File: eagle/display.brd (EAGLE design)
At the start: 100 x 20 mm, 6 parts

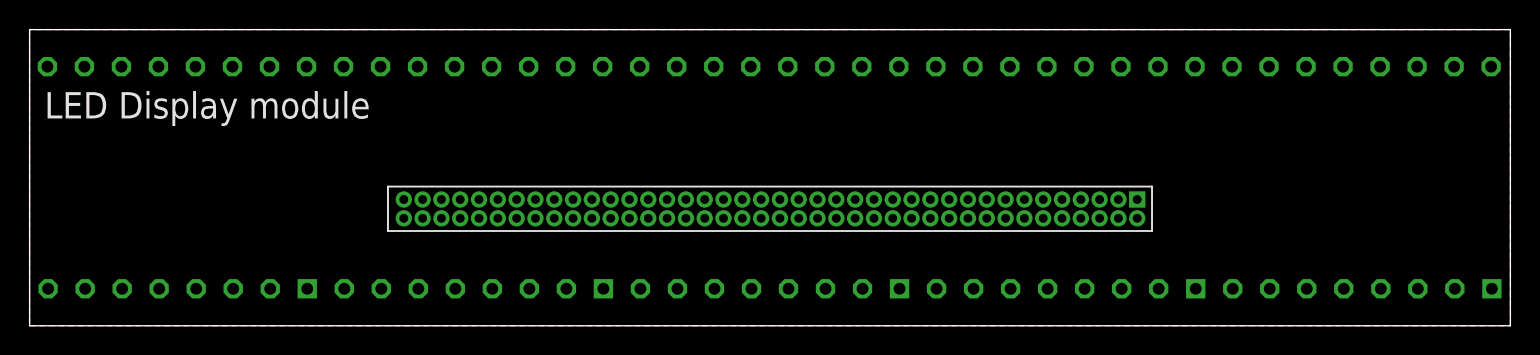
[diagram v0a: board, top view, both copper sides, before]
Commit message: removed pinhead
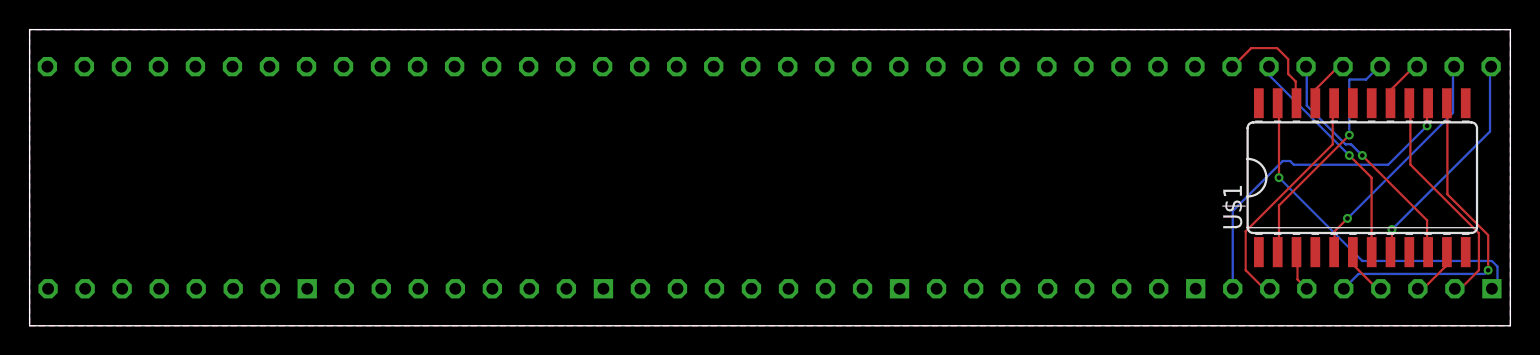
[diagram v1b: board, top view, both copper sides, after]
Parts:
- removed U$6: PINHD-2X40FEMALE, pinhead-1.27:FEMALE-2X40
- added U$1: MAX7219CWG, max7219:SO24L
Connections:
- removed net MX1_ANODE1: U$6.P$1
- removed net MX1_ANODE2: U$6.P$3
- removed net MX1_ANODE3: U$6.P$5
- removed net MX1_ANODE4: U$6.P$7
- removed net MX1_ANODE5: U$6.P$9
- removed net MX1_ANODE6: U$6.P$11
- removed net MX1_ANODE7: U$6.P$13
- removed net MX1_ANODE8: U$6.P$15
- removed net MX1_CATHODE1: U$6.P$2
- removed net MX1_CATHODE2: U$6.P$4
- removed net MX1_CATHODE3: U$6.P$6
- removed net MX1_CATHODE4: U$6.P$8
- removed net MX1_CATHODE5: U$6.P$10
- removed net MX1_CATHODE6: U$6.P$12
- removed net MX1_CATHODE7: U$6.P$14
- removed net MX1_CATHODE8: U$6.P$16
- removed net MX2_ANODE1: U$6.P$17
- removed net MX2_ANODE2: U$6.P$19
- removed net MX2_ANODE3: U$6.P$21
- removed net MX2_ANODE4: U$6.P$23
- removed net MX2_ANODE5: U$6.P$25
- removed net MX2_ANODE6: U$6.P$27
- removed net MX2_ANODE7: U$6.P$29
- removed net MX2_ANODE8: U$6.P$31
- removed net MX2_CATHODE1: U$6.P$18
- removed net MX2_CATHODE2: U$6.P$20
- removed net MX2_CATHODE3: U$6.P$22
- removed net MX2_CATHODE4: U$6.P$24
- removed net MX2_CATHODE5: U$6.P$26
- removed net MX2_CATHODE6: U$6.P$28
- removed net MX2_CATHODE7: U$6.P$30
- removed net MX2_CATHODE8: U$6.P$32
- removed net MX3_ANODE1: U$6.P$33
- removed net MX3_ANODE2: U$6.P$35
- removed net MX3_ANODE3: U$6.P$37
- removed net MX3_ANODE4: U$6.P$39
- removed net MX3_ANODE5: U$6.P$41
- removed net MX3_ANODE6: U$6.P$43
- removed net MX3_ANODE7: U$6.P$45
- removed net MX3_ANODE8: U$6.P$47
- removed net MX3_CATHODE1: U$6.P$34
- removed net MX3_CATHODE2: U$6.P$36
- removed net MX3_CATHODE3: U$6.P$38
- removed net MX3_CATHODE4: U$6.P$40
- removed net MX3_CATHODE5: U$6.P$42
- removed net MX3_CATHODE6: U$6.P$44
- removed net MX3_CATHODE7: U$6.P$46
- removed net MX3_CATHODE8: U$6.P$48
- removed net MX4_ANODE1: U$6.P$49
- removed net MX4_ANODE2: U$6.P$51
- removed net MX4_ANODE3: U$6.P$53
- removed net MX4_ANODE4: U$6.P$55
- removed net MX4_ANODE5: U$6.P$57
- removed net MX4_ANODE6: U$6.P$59
- removed net MX4_ANODE7: U$6.P$61
- removed net MX4_ANODE8: U$6.P$63
- removed net MX4_CATHODE1: U$6.P$50
- removed net MX4_CATHODE2: U$6.P$52
- removed net MX4_CATHODE3: U$6.P$54
- removed net MX4_CATHODE4: U$6.P$56
- removed net MX4_CATHODE5: U$6.P$58
- removed net MX4_CATHODE6: U$6.P$60
- removed net MX4_CATHODE7: U$6.P$62
- removed net MX4_CATHODE8: U$6.P$64
- removed net MX5_ANODE1: U$6.P$65
- removed net MX5_ANODE2: U$6.P$67
- removed net MX5_ANODE3: U$6.P$69
- removed net MX5_ANODE4: U$6.P$71
- removed net MX5_ANODE5: U$6.P$73
- removed net MX5_ANODE6: U$6.P$75
- removed net MX5_ANODE7: U$6.P$77
- removed net MX5_ANODE8: U$6.P$79
- removed net MX5_CATHODE1: U$6.P$66
- removed net MX5_CATHODE2: U$6.P$68
- removed net MX5_CATHODE3: U$6.P$70
- removed net MX5_CATHODE4: U$6.P$72
- removed net MX5_CATHODE5: U$6.P$74
- removed net MX5_CATHODE6: U$6.P$76
- removed net MX5_CATHODE7: U$6.P$78
- removed net MX5_CATHODE8: U$6.P$80
- new net ANODE1: LED1.P$5, U$1.14
- new net ANODE2: LED1.P$2, U$1.16
- new net ANODE3: LED1.P$7, U$1.20
- new net ANODE4: LED1.P$1, U$1.23
- new net ANODE5: LED1.P$12, U$1.21
- new net ANODE6: LED1.P$8, U$1.15
- new net ANODE7: LED1.P$14, U$1.17
- new net ANODE8: LED1.P$9, U$1.22
- new net CATHODE1: LED1.P$13, U$1.2
- new net CATHODE2: LED1.P$3, U$1.11
- new net CATHODE3: LED1.P$4, U$1.6
- new net CATHODE4: LED1.P$10, U$1.7
- new net CATHODE5: LED1.P$6, U$1.3
- new net CATHODE6: LED1.P$11, U$1.10
- new net CATHODE7: LED1.P$15, U$1.5
- new net CATHODE8: LED1.P$16, U$1.8
- new net GND: U$1.4, U$1.9
- new net VCC: U$1.19
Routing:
- net ANODE4: track 0.00 -> 24.2 mm, vias 0 -> 1
- net ANODE1: track 0.00 -> 22.7 mm, vias 0 -> 1
- net ANODE6: track 0.00 -> 22.5 mm, vias 0 -> 1
- net CATHODE6: track 0.00 -> 16.2 mm, vias 0 -> 1
- net CATHODE1: track 0.00 -> 16.1 mm, vias 0 -> 1
- net CATHODE7: track 0.00 -> 15.9 mm, vias 0 -> 1
- net ANODE3: track 0.00 -> 15.9 mm
- net CATHODE4: track 0.00 -> 15.4 mm, vias 0 -> 1
- net CATHODE8: track 0.00 -> 15.4 mm, vias 0 -> 1
- net ANODE2: track 0.00 -> 15.4 mm
- net ANODE8: track 0.00 -> 7.82 mm
- net CATHODE2: track 0.00 -> 3.50 mm
- net ANODE5: track 0.00 -> 3.43 mm
- net CATHODE3: track 0.00 -> 3.39 mm
- net ANODE7: track 0.00 -> 3.33 mm
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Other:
- board text removed: "LED Display module"

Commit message: display board
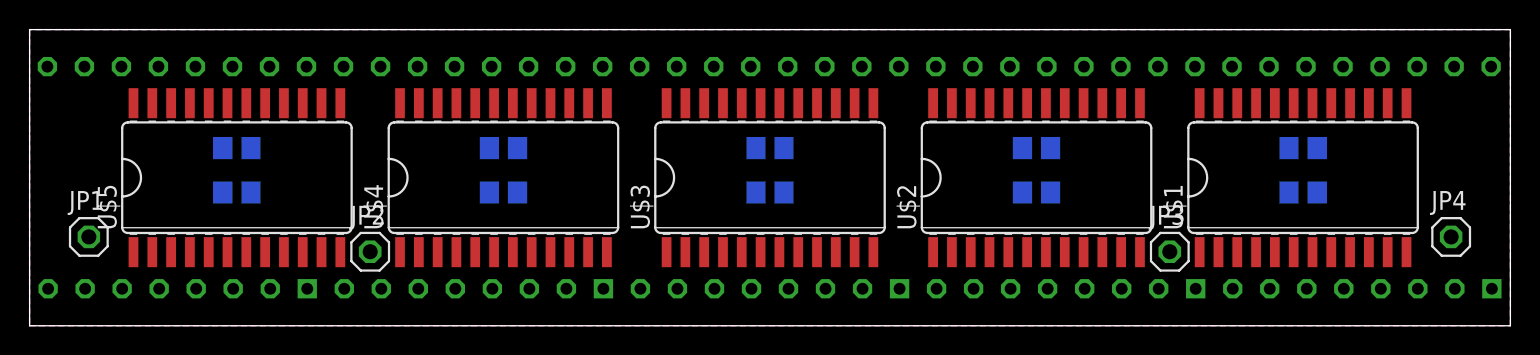
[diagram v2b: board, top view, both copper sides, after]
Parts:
- added C1, C2, C3, C4, C5: 100u, rcl:C0805
- added JP1: CLK, pinhead:1X01
- added JP2: LOAD, pinhead:1X01
- added JP3: DIN, pinhead:1X01
- added JP4: VCC, pinhead:1X01
- added R1, R2, R3, R4, R5: 10k, rcl:R0805
- added U$2, U$3, U$4, U$5: MAX7219CWG, max7219:SO24L
- moved U$1 4.00 mm to (86.0, 10.0)
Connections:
- net ANODE1 renamed MATRIX1_ANODE1
- net ANODE2 renamed MATRIX1_ANODE2
- net ANODE3 renamed MATRIX1_ANODE3
- net ANODE4 renamed MATRIX1_ANODE4
- net ANODE5 renamed MATRIX1_ANODE5
- net ANODE6 renamed MATRIX1_ANODE6
- net ANODE7 renamed MATRIX1_ANODE7
- net ANODE8 renamed MATRIX1_ANODE8
- net CATHODE1 renamed MATRIX1_CATHODE1
- net CATHODE2 renamed MATRIX1_CATHODE2
- net CATHODE3 renamed MATRIX1_CATHODE3
- net CATHODE4 renamed MATRIX1_CATHODE4
- net CATHODE5 renamed MATRIX1_CATHODE5
- net CATHODE6 renamed MATRIX1_CATHODE6
- net CATHODE7 renamed MATRIX1_CATHODE7
- net CATHODE8 renamed MATRIX1_CATHODE8
- new net CLK: JP1.1, U$1.13, U$2.13, U$3.13, U$4.13, U$5.13
- new net D1: U$1.24, U$2.1
- new net D2: U$2.24, U$3.1
- new net D3: U$3.24, U$4.1
- new net D4: U$4.24, U$5.1
- new net D5: U$5.24
- new net DIN: JP3.1, U$1.1
- new net LD: JP2.1, U$1.12, U$2.12, U$3.12, U$4.12, U$5.12
- new net MATRIX2_ANODE1: LED2.P$5, U$2.14
- new net MATRIX2_ANODE2: LED2.P$2, U$2.16
- new net MATRIX2_ANODE3: LED2.P$7, U$2.20
- new net MATRIX2_ANODE4: LED2.P$1, U$2.23
- new net MATRIX2_ANODE5: LED2.P$12, U$2.21
- new net MATRIX2_ANODE6: LED2.P$8, U$2.15
- new net MATRIX2_ANODE7: LED2.P$14, U$2.17
- new net MATRIX2_ANODE8: LED2.P$9, U$2.22
- new net MATRIX2_CATHODE1: LED2.P$13, U$2.2
- new net MATRIX2_CATHODE2: LED2.P$3, U$2.11
- new net MATRIX2_CATHODE3: LED2.P$4, U$2.6
- new net MATRIX2_CATHODE4: LED2.P$10, U$2.7
- new net MATRIX2_CATHODE5: LED2.P$6, U$2.3
- new net MATRIX2_CATHODE6: LED2.P$11, U$2.10
- new net MATRIX2_CATHODE7: LED2.P$15, U$2.5
- new net MATRIX2_CATHODE8: LED2.P$16, U$2.8
- new net MATRIX3_ANODE1: LED3.P$5, U$3.14
- new net MATRIX3_ANODE2: LED3.P$2, U$3.16
- new net MATRIX3_ANODE3: LED3.P$7, U$3.20
- new net MATRIX3_ANODE4: LED3.P$1, U$3.23
- new net MATRIX3_ANODE5: LED3.P$12, U$3.21
- new net MATRIX3_ANODE6: LED3.P$8, U$3.15
- new net MATRIX3_ANODE7: LED3.P$14, U$3.17
- new net MATRIX3_ANODE8: LED3.P$9, U$3.22
- new net MATRIX3_CATHODE1: LED3.P$13, U$3.2
- new net MATRIX3_CATHODE2: LED3.P$3, U$3.11
- new net MATRIX3_CATHODE3: LED3.P$4, U$3.6
- new net MATRIX3_CATHODE4: LED3.P$10, U$3.7
- new net MATRIX3_CATHODE5: LED3.P$6, U$3.3
- new net MATRIX3_CATHODE6: LED3.P$11, U$3.10
- new net MATRIX3_CATHODE7: LED3.P$15, U$3.5
- new net MATRIX3_CATHODE8: LED3.P$16, U$3.8
- new net MATRIX4_ANODE1: LED4.P$5, U$4.14
- new net MATRIX4_ANODE2: LED4.P$2, U$4.16
- new net MATRIX4_ANODE3: LED4.P$7, U$4.20
- new net MATRIX4_ANODE4: LED4.P$1, U$4.23
- new net MATRIX4_ANODE5: LED4.P$12, U$4.21
- new net MATRIX4_ANODE6: LED4.P$8, U$4.15
- new net MATRIX4_ANODE7: LED4.P$14, U$4.17
- new net MATRIX4_ANODE8: LED4.P$9, U$4.22
- new net MATRIX4_CATHODE1: LED4.P$13, U$4.2
- new net MATRIX4_CATHODE2: LED4.P$3, U$4.11
- new net MATRIX4_CATHODE3: LED4.P$4, U$4.6
- new net MATRIX4_CATHODE4: LED4.P$10, U$4.7
- new net MATRIX4_CATHODE5: LED4.P$6, U$4.3
- new net MATRIX4_CATHODE6: LED4.P$11, U$4.10
- new net MATRIX4_CATHODE7: LED4.P$15, U$4.5
- new net MATRIX4_CATHODE8: LED4.P$16, U$4.8
- new net MATRIX5_ANODE1: LED5.P$5, U$5.14
- new net MATRIX5_ANODE2: LED5.P$2, U$5.16
- new net MATRIX5_ANODE3: LED5.P$7, U$5.20
- new net MATRIX5_ANODE4: LED5.P$1, U$5.23
- new net MATRIX5_ANODE5: LED5.P$12, U$5.21
- new net MATRIX5_ANODE6: LED5.P$8, U$5.15
- new net MATRIX5_ANODE7: LED5.P$14, U$5.17
- new net MATRIX5_ANODE8: LED5.P$9, U$5.22
- new net MATRIX5_CATHODE1: LED5.P$13, U$5.2
- new net MATRIX5_CATHODE2: LED5.P$3, U$5.11
- new net MATRIX5_CATHODE3: LED5.P$4, U$5.6
- new net MATRIX5_CATHODE4: LED5.P$10, U$5.7
- new net MATRIX5_CATHODE5: LED5.P$6, U$5.3
- new net MATRIX5_CATHODE6: LED5.P$11, U$5.10
- new net MATRIX5_CATHODE7: LED5.P$15, U$5.5
- new net MATRIX5_CATHODE8: LED5.P$16, U$5.8
- new net N$1: R5.2, U$5.18
- new net N$10: R2.2, U$2.18
- new net N$15: R3.2, U$3.18
- new net N$20: R4.2, U$4.18
- new net N$5: R1.2, U$1.18
- net GND: now also C1.2, C2.2, C3.2, C4.2, C5.2, U$2.4, U$2.9, U$3.4, U$3.9, U$4.4, U$4.9, U$5.4, U$5.9
- net VCC: now also C1.1, C2.1, C3.1, C4.1, C5.1, JP4.1, R1.1, R2.1, R3.1, R4.1, R5.1, U$2.19, U$3.19, U$4.19, U$5.19
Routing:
- net MATRIX1_ANODE4: track 24.2 -> 0.00 mm, vias 1 -> 0
- net MATRIX1_ANODE1: track 22.7 -> 0.00 mm, vias 1 -> 0
- net MATRIX1_ANODE6: track 22.5 -> 0.00 mm, vias 1 -> 0
- net MATRIX1_CATHODE6: track 16.2 -> 0.00 mm, vias 1 -> 0
- net MATRIX1_CATHODE1: track 16.1 -> 0.00 mm, vias 1 -> 0
- net MATRIX1_CATHODE7: track 15.9 -> 0.00 mm, vias 1 -> 0
- net MATRIX1_ANODE3: track 15.9 -> 0.00 mm
- net MATRIX1_CATHODE4: track 15.4 -> 0.00 mm, vias 1 -> 0
- net MATRIX1_CATHODE8: track 15.4 -> 0.00 mm, vias 1 -> 0
- net MATRIX1_ANODE2: track 15.4 -> 0.00 mm
- net MATRIX1_ANODE8: track 7.82 -> 0.00 mm
- net MATRIX1_CATHODE2: track 3.50 -> 0.00 mm
- net MATRIX1_ANODE5: track 3.43 -> 0.00 mm
- net MATRIX1_CATHODE3: track 3.39 -> 0.00 mm
- net MATRIX1_ANODE7: track 3.33 -> 0.00 mm
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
